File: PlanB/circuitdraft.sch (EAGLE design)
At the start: 20 parts, among them Q1 16 MHz

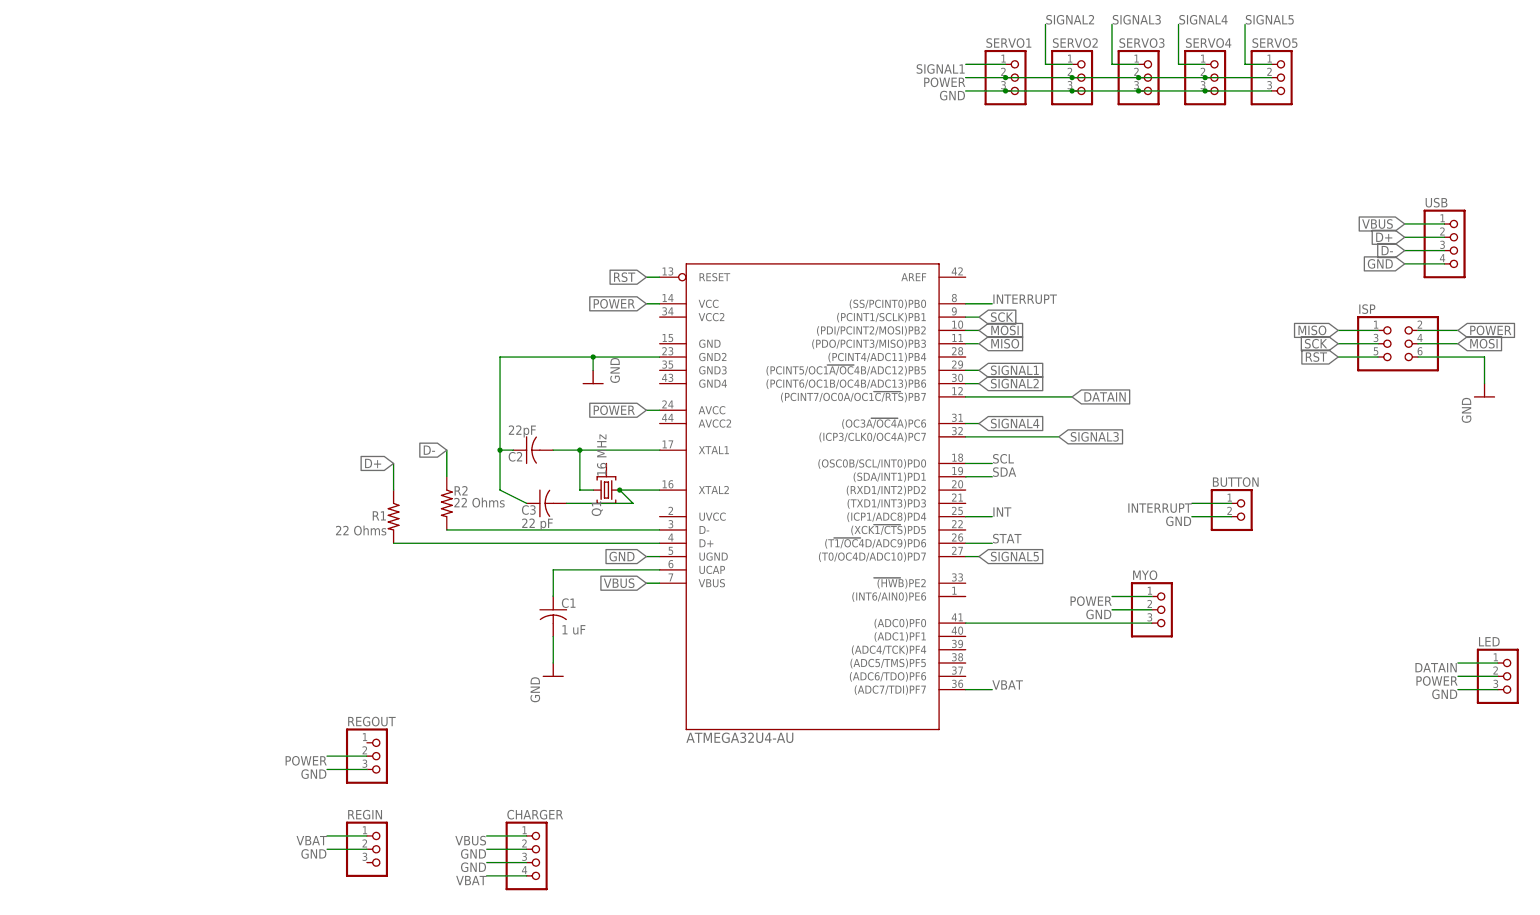
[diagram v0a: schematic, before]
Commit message: added biggnd and bigpower for large traces
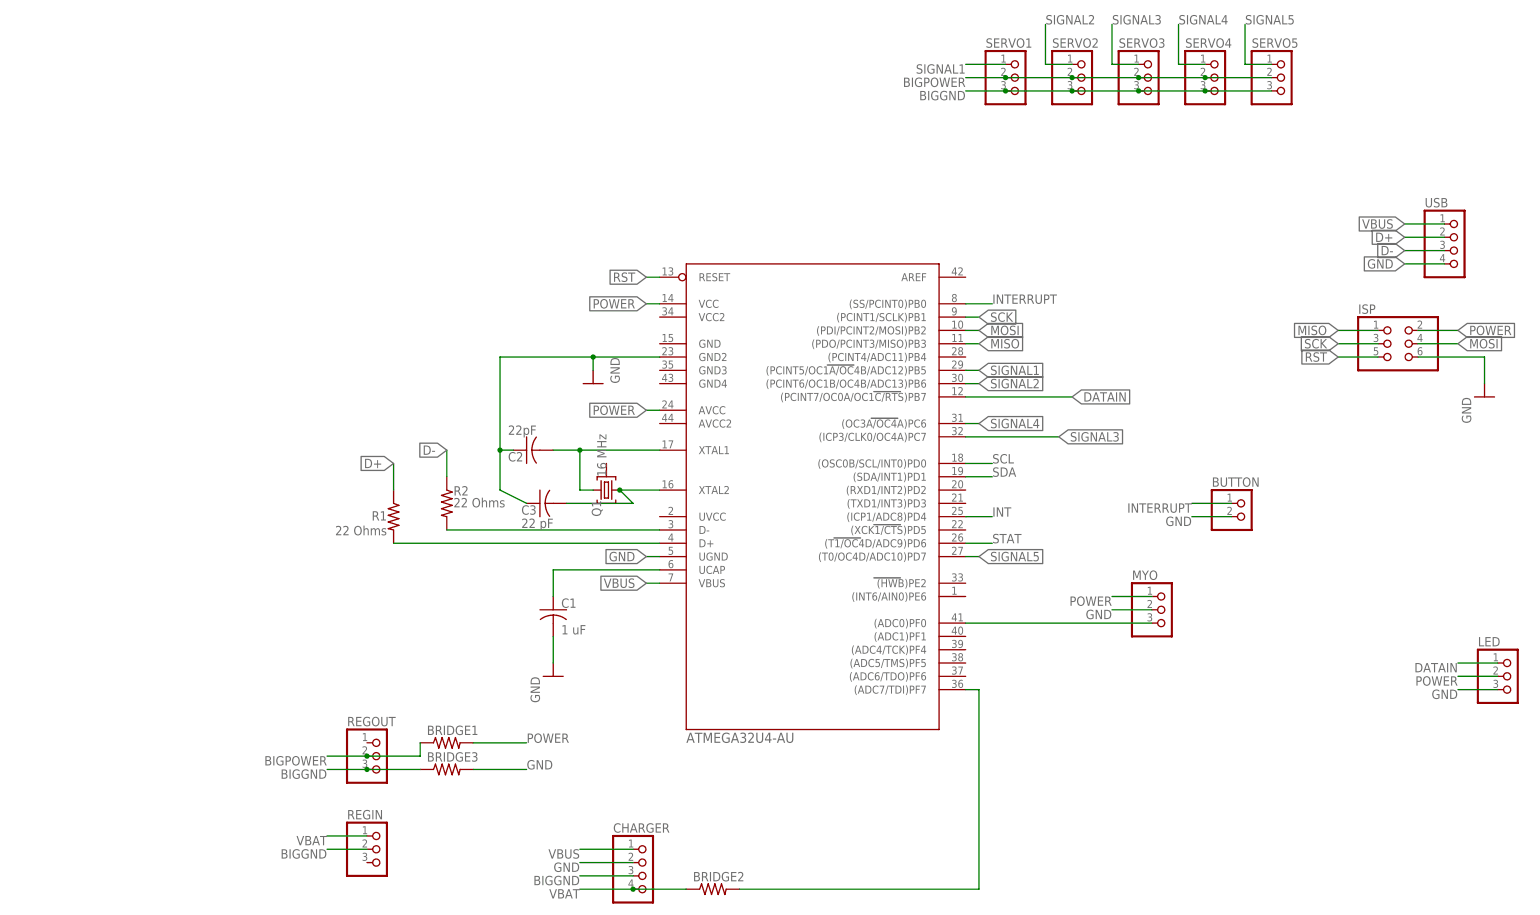
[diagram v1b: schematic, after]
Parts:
- added BRIDGE1, BRIDGE2, BRIDGE3: (no value), rcl:R-US_M0805
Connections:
- new net BIGGND: BRIDGE3.1, CHARGER.3, REGIN.2, REGOUT.3, SERVO1.3, SERVO2.3, SERVO3.3, SERVO4.3, SERVO5.3
- new net BIGPOWER: BRIDGE1.1, REGOUT.2, SERVO1.2, SERVO2.2, SERVO3.2, SERVO4.2, SERVO5.2
- new net N$9: BRIDGE2.2, U$1.(ADC7/TDI)PF7
- net GND: now also BRIDGE3.2; no longer CHARGER.3, REGIN.2, REGOUT.3, SERVO1.3, SERVO2.3, SERVO3.3, SERVO4.3, SERVO5.3
- net POWER: now also BRIDGE1.2; no longer REGOUT.2, SERVO1.2, SERVO2.2, SERVO3.2, SERVO4.2, SERVO5.2
- net VBAT: now also BRIDGE2.1; no longer U$1.(ADC7/TDI)PF7
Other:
- moved on the sheet: CHARGER

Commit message: more ajustments
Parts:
- removed BRIDGE3: (no value), rcl:R-US_M0805
- removed Q1: 16 MHz, crystal:10G7A-12.5KHZ
- removed REGIN, REGOUT: (no value), pinhead:PINHD-1X3
- added REGGNDIN, REGGNDOUT, REGVIN, REGVOUT: (no value), pinhead:PINHD-1X1
- added Y1: CY16BPS, SamacSys_Parts:CY16BPS
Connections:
- removed net BIGGND: BRIDGE3.1, CHARGER.3, REGIN.2, REGOUT.3, SERVO1.3, SERVO2.3, SERVO3.3, SERVO4.3, SERVO5.3
- net BIGPOWER: now also REGVOUT.1; no longer REGOUT.2
- net GND: now also CHARGER.3, REGGNDIN.1, REGGNDOUT.1, SERVO1.3, SERVO2.3, SERVO3.3, SERVO4.3, SERVO5.3, U$1.GND, U$1.GND3, U$1.GND4; no longer BRIDGE3.2
- net N$5: now also C2.2, U$1.XTAL1, Y1.2; no longer C3.2, Q1.1, U$1.XTAL2
- net N$6: now also C3.2, U$1.XTAL2, Y1.1; no longer C2.2, Q1.3, U$1.XTAL1
- net POWER: now also U$1.UVCC
- net VBAT: now also REGVIN.1; no longer REGIN.1
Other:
- moved on the sheet: BRIDGE1, C2, C3

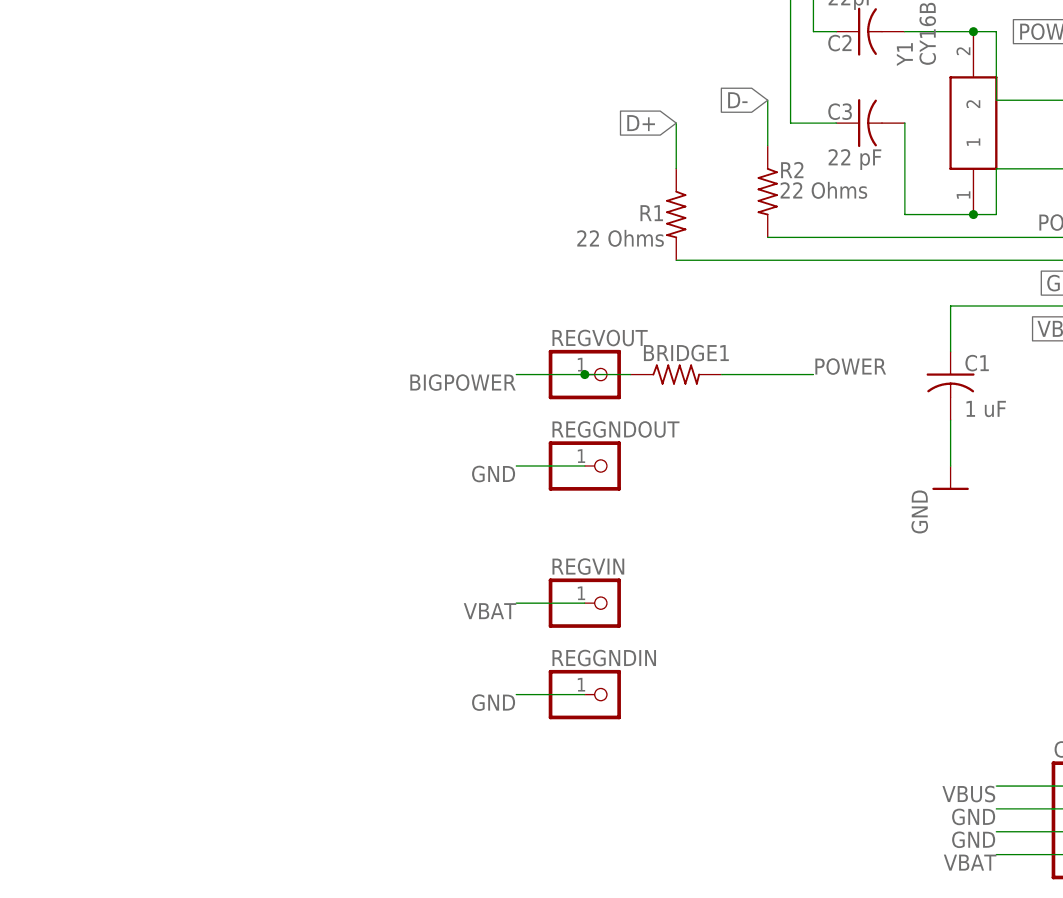
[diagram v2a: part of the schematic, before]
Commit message: refined board and fixed locations and orintations
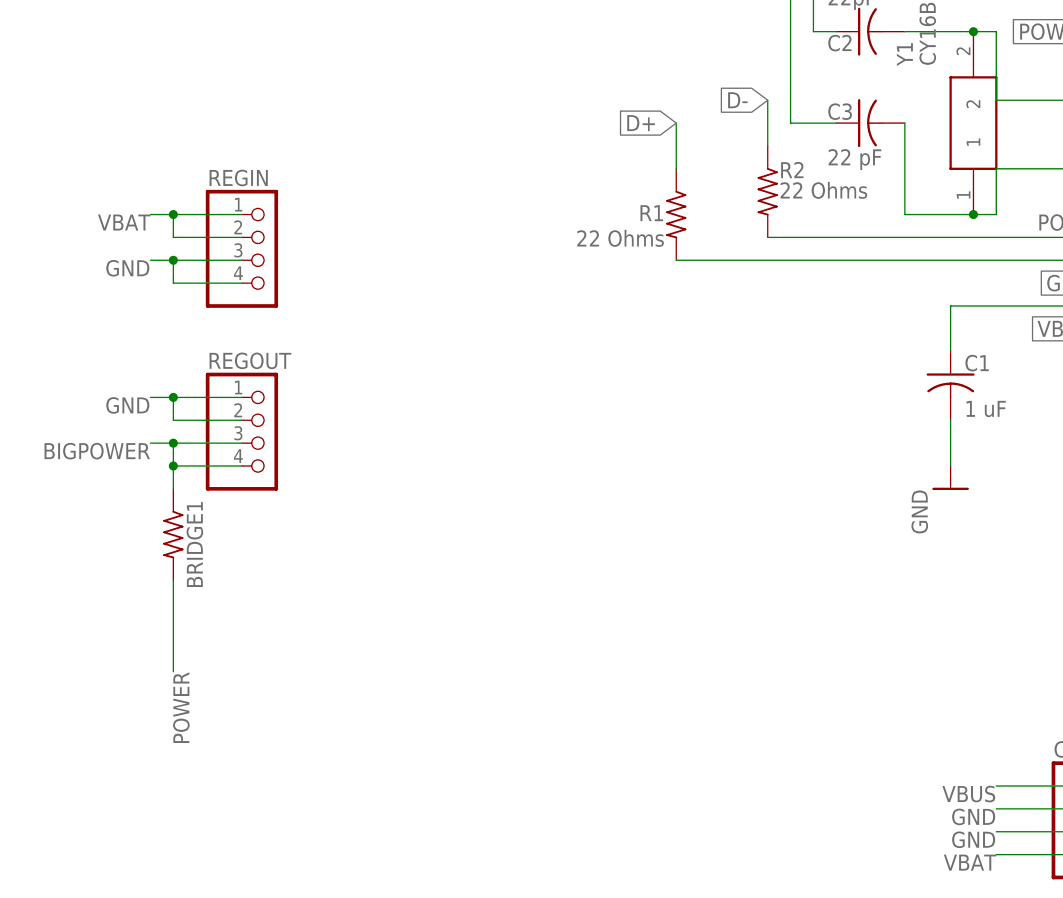
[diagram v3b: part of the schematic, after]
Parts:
- removed REGGNDIN, REGGNDOUT, REGVIN, REGVOUT: (no value), pinhead:PINHD-1X1
- added REGIN, REGOUT: (no value), pinhead:PINHD-1X4
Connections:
- net BIGPOWER: now also REGOUT.3, REGOUT.4; no longer REGVOUT.1
- net GND: now also REGIN.3, REGIN.4, REGOUT.1, REGOUT.2; no longer REGGNDIN.1, REGGNDOUT.1
- net VBAT: now also REGIN.1, REGIN.2; no longer REGVIN.1
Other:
- moved on the sheet: BRIDGE1
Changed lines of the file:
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@@
 <?xml version="1.0" encoding="utf-8"?>
 <!DOCTYPE eagle SYSTEM "eagle.dtd">
-<eagle version="9.5.1">
+<eagle version="9.5.2">
 <drawing>
 <settings>
@@
 <part name="BRIDGE1" library="rcl" library_urn="urn:adsk.eagle:library:334" deviceset="R-US_" device="M0805" package3d_urn="urn:adsk.eagle:package:23556/2"/>
 <part name="BRIDGE2" library="rcl" library_urn="urn:adsk.eagle:library:334" deviceset="R-US_" device="M0805" package3d_urn="urn:adsk.eagle:package:23556/2"/>
-<part name="REGVOUT" library="pinhead" library_urn="urn:adsk.eagle:library:325" deviceset="PINHD-1X1" device="" package3d_urn="urn:adsk.eagle:package:22485/2"/>
-<part name="REGGNDOUT" library="pinhead" library_urn="urn:adsk.eagle:library:325" deviceset="PINHD-1X1" device="" package3d_urn="urn:adsk.eagle:package:22485/2"/>
-<part name="REGVIN" library="pinhead" library_urn="urn:adsk.eagle:library:325" deviceset="PINHD-1X1" device="" package3d_urn="urn:adsk.eagle:package:22485/2"/>
-<part name="REGGNDIN" library="pinhead" library_urn="urn:adsk.eagle:library:325" deviceset="PINHD-1X1" device="" package3d_urn="urn:adsk.eagle:package:22485/2"/>
 <part name="Y1" library="SamacSys_Parts" deviceset="CY16BPS" device=""/>
+<part name="REGIN" library="pinhead" library_urn="urn:adsk.eagle:library:325" deviceset="PINHD-1X4" device="" package3d_urn="urn:adsk.eagle:package:22407/2"/>
+<part name="REGOUT" library="pinhead" library_urn="urn:adsk.eagle:library:325" deviceset="PINHD-1X4" device="" package3d_urn="urn:adsk.eagle:package:22407/2"/>
 </parts>
 <sheets>
@@
 <attribute name="VALUE" x="227.33" y="111.76" size="1.778" layer="96"/>
 </instance>
-<instance part="BRIDGE1" gate="G$1" x="86.36" y="119.38" smashed="yes">
-<attribute name="NAME" x="82.55" y="120.8786" size="1.778" layer="95"/>
-<attribute name="VALUE" x="82.55" y="116.078" size="1.778" layer="96"/>
+<instance part="BRIDGE1" gate="G$1" x="30.48" y="101.6" smashed="yes" rot="R270">
+<attribute name="NAME" x="31.9786" y="105.41" size="1.778" layer="95" rot="R270"/>
+<attribute name="VALUE" x="27.178" y="105.41" size="1.778" layer="96" rot="R270"/>
 </instance>
 <instance part="BRIDGE2" gate="G$1" x="147.32" y="66.04" smashed="yes">
@@
 <attribute name="VALUE" x="143.51" y="62.738" size="1.778" layer="96"/>
 </instance>
-<instance part="REGVOUT" gate="G$1" x="78.74" y="119.38" smashed="yes">
-<attribute name="NAME" x="72.39" y="122.555" size="1.778" layer="95"/>
-<attribute name="VALUE" x="72.39" y="114.3" size="1.778" layer="96"/>
-</instance>
-<instance part="REGGNDOUT" gate="G$1" x="78.74" y="109.22" smashed="yes">
-<attribute name="NAME" x="72.39" y="112.395" size="1.778" layer="95"/>
-<attribute name="VALUE" x="72.39" y="104.14" size="1.778" layer="96"/>
-</instance>
-<instance part="REGVIN" gate="G$1" x="78.74" y="93.98" smashed="yes">
-<attribute name="NAME" x="72.39" y="97.155" size="1.778" layer="95"/>
-<attribute name="VALUE" x="72.39" y="88.9" size="1.778" layer="96"/>
-</instance>
-<instance part="REGGNDIN" gate="G$1" x="78.74" y="83.82" smashed="yes">
-<attribute name="NAME" x="72.39" y="86.995" size="1.778" layer="95"/>
-<attribute name="VALUE" x="72.39" y="78.74" size="1.778" layer="96"/>
-</instance>
 <instance part="Y1" gate="G$1" x="119.38" y="137.16" smashed="yes" rot="R90">
 <attribute name="NAME" x="111.76" y="153.67" size="1.778" layer="95" rot="R90" align="center-left"/>
 <attribute name="VALUE" x="114.3" y="153.67" size="1.778" layer="96" rot="R90" align="center-left"/>
+</instance>
+<instance part="REGIN" gate="A" x="40.64" y="132.08" smashed="yes">
+<attribute name="NAME" x="34.29" y="140.335" size="1.778" layer="95"/>
+<attribute name="VALUE" x="34.29" y="124.46" size="1.778" layer="96"/>
+</instance>
+<instance part="REGOUT" gate="A" x="40.64" y="111.76" smashed="yes">
+<attribute name="NAME" x="34.29" y="120.015" size="1.778" layer="95"/>
+<attribute name="VALUE" x="34.29" y="104.14" size="1.778" layer="96"/>
 </instance>
 </instances>
@@
 <segment>
 <pinref part="BRIDGE1" gate="G$1" pin="2"/>
-<wire x1="91.44" y1="119.38" x2="101.6" y2="119.38" width="0.1524" layer="91"/>
-<label x="101.6" y="119.38" size="1.778" layer="95"/>
+<wire x1="30.48" y1="96.52" x2="30.48" y2="86.36" width="0.1524" layer="91"/>
+<label x="30.48" y="86.36" size="1.778" layer="95" rot="R270"/>
 </segment>
 <segment>
@@
 </segment>
 <segment>
-<pinref part="REGGNDOUT" gate="G$1" pin="1"/>
-<wire x1="76.2" y1="109.22" x2="68.58" y2="109.22" width="0.1524" layer="91"/>
-<label x="68.58" y="109.22" size="1.778" layer="95" rot="R180"/>
-</segment>
-<segment>
-<pinref part="REGGNDIN" gate="G$1" pin="1"/>
-<wire x1="76.2" y1="83.82" x2="68.58" y2="83.82" width="0.1524" layer="91"/>
-<label x="68.58" y="83.82" size="1.778" layer="95" rot="R180"/>
-</segment>
-<segment>
 <pinref part="C2" gate="G$1" pin="1"/>
 <wire x1="104.14" y1="157.48" x2="101.6" y2="157.48" width="0.1524" layer="91"/>
@@
 <wire x1="137.16" y1="162.56" x2="129.54" y2="162.56" width="0.1524" layer="91"/>
 <label x="129.54" y="162.56" size="1.778" layer="95"/>
+</segment>
+<segment>
+<pinref part="REGIN" gate="A" pin="3"/>
+<wire x1="38.1" y1="132.08" x2="30.48" y2="132.08" width="0.1524" layer="91"/>
+<pinref part="REGIN" gate="A" pin="4"/>
+<wire x1="30.48" y1="132.08" x2="27.94" y2="132.08" width="0.1524" layer="91"/>
+<wire x1="30.48" y1="132.08" x2="30.48" y2="129.54" width="0.1524" layer="91"/>
+<wire x1="30.48" y1="129.54" x2="38.1" y2="129.54" width="0.1524" layer="91"/>
+<junction x="30.48" y="132.08"/>
+<label x="27.94" y="132.08" size="1.778" layer="95" rot="R180"/>
+</segment>
+<segment>
+<pinref part="REGOUT" gate="A" pin="1"/>
+<wire x1="38.1" y1="116.84" x2="30.48" y2="116.84" width="0.1524" layer="91"/>
+<wire x1="27.94" y1="116.84" x2="30.48" y2="116.84" width="0.1524" layer="91"/>
+<pinref part="REGOUT" gate="A" pin="2"/>
+<wire x1="30.48" y1="116.84" x2="30.48" y2="114.3" width="0.1524" layer="91"/>
+<wire x1="30.48" y1="114.3" x2="38.1" y2="114.3" width="0.1524" layer="91"/>
+<junction x="30.48" y="116.84"/>
+<label x="27.94" y="116.84" size="1.778" layer="95" rot="R180"/>
 </segment>
 </net>
@@
 </segment>
 <segment>
-<pinref part="REGVIN" gate="G$1" pin="1"/>
-<wire x1="76.2" y1="93.98" x2="68.58" y2="93.98" width="0.1524" layer="91"/>
-<label x="68.58" y="93.98" size="1.778" layer="95" rot="R180"/>
+<pinref part="REGIN" gate="A" pin="1"/>
+<wire x1="38.1" y1="137.16" x2="30.48" y2="137.16" width="0.1524" layer="91"/>
+<pinref part="REGIN" gate="A" pin="2"/>
+<wire x1="30.48" y1="137.16" x2="30.48" y2="134.62" width="0.1524" layer="91"/>
+<wire x1="30.48" y1="134.62" x2="38.1" y2="134.62" width="0.1524" layer="91"/>
+<wire x1="30.48" y1="137.16" x2="27.94" y2="137.16" width="0.1524" layer="91"/>
+<junction x="30.48" y="137.16"/>
+<label x="27.94" y="137.16" size="1.778" layer="95" rot="R180"/>
 </segment>
 </net>
@@
 </segment>
 <segment>
-<pinref part="REGVOUT" gate="G$1" pin="1"/>
-<wire x1="76.2" y1="119.38" x2="68.58" y2="119.38" width="0.1524" layer="91"/>
-<label x="68.58" y="119.38" size="1.778" layer="95" rot="R180"/>
+<pinref part="REGOUT" gate="A" pin="3"/>
+<wire x1="38.1" y1="111.76" x2="30.48" y2="111.76" width="0.1524" layer="91"/>
+<pinref part="REGOUT" gate="A" pin="4"/>
+<wire x1="30.48" y1="111.76" x2="27.94" y2="111.76" width="0.1524" layer="91"/>
+<wire x1="38.1" y1="109.22" x2="30.48" y2="109.22" width="0.1524" layer="91"/>
+<wire x1="30.48" y1="109.22" x2="30.48" y2="111.76" width="0.1524" layer="91"/>
+<junction x="30.48" y="111.76"/>
+<label x="27.94" y="111.76" size="1.778" layer="95" rot="R180"/>
 <pinref part="BRIDGE1" gate="G$1" pin="1"/>
-<wire x1="76.2" y1="119.38" x2="81.28" y2="119.38" width="0.1524" layer="91"/>
-<junction x="76.2" y="119.38"/>
-</segment>
-</net>
+<wire x1="30.48" y1="109.22" x2="30.48" y2="106.68" width="0.1524" layer="91"/>
+<junction x="30.48" y="109.22"/>
+</segment>
+</net>

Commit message: final refinement
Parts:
- C1: device rcl:C-US025-024X044 -> rcl:C-US050-024X044
- R1, R2: device rcl:R-US_0204/7 -> rcl:R-US_0207/10
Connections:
- net INTERRUPT: now also U$1.(INT6/AIN0)PE6; no longer U$1.(SS/PCINT0)PB0
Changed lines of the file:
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@@
 <?xml version="1.0" encoding="utf-8"?>
 <!DOCTYPE eagle SYSTEM "eagle.dtd">
-<eagle version="9.5.2">
+<eagle version="9.5.1">
 <drawing>
 <settings>
@@
 <part name="U$1" library="mega32U4" deviceset="ATMEGA32U4-AU" device=""/>
 <part name="USB" library="pinhead" library_urn="urn:adsk.eagle:library:325" deviceset="PINHD-1X4" device="" package3d_urn="urn:adsk.eagle:package:22407/2"/>
-<part name="C1" library="rcl" library_urn="urn:adsk.eagle:library:334" deviceset="C-US" device="025-024X044" package3d_urn="urn:adsk.eagle:package:23630/1" value="1 uF"/>
+<part name="C1" library="rcl" library_urn="urn:adsk.eagle:library:334" deviceset="C-US" device="050-024X044" package3d_urn="urn:adsk.eagle:package:23643/1" value="1 uF"/>
 <part name="AGND1" library="supply1" library_urn="urn:adsk.eagle:library:371" deviceset="GND" device=""/>
-<part name="R1" library="rcl" library_urn="urn:adsk.eagle:library:334" deviceset="R-US_" device="0204/7" package3d_urn="urn:adsk.eagle:package:23498/2" value="22 Ohms"/>
-<part name="R2" library="rcl" library_urn="urn:adsk.eagle:library:334" deviceset="R-US_" device="0204/7" package3d_urn="urn:adsk.eagle:package:23498/2" value="22 Ohms"/>
+<part name="R1" library="rcl" library_urn="urn:adsk.eagle:library:334" deviceset="R-US_" device="0207/10" package3d_urn="urn:adsk.eagle:package:23491/2" value="22 Ohms"/>
+<part name="R2" library="rcl" library_urn="urn:adsk.eagle:library:334" deviceset="R-US_" device="0207/10" package3d_urn="urn:adsk.eagle:package:23491/2" value="22 Ohms"/>
 <part name="ISP" library="pinhead" library_urn="urn:adsk.eagle:library:325" deviceset="PINHD-2X3" device="" package3d_urn="urn:adsk.eagle:package:22462/2"/>
 <part name="AGND3" library="supply1" library_urn="urn:adsk.eagle:library:371" deviceset="GND" device=""/>
@@
 <net name="INTERRUPT" class="0">
 <segment>
-<pinref part="U$1" gate="G$1" pin="(SS/PCINT0)PB0"/>
-<wire x1="195.58" y1="177.8" x2="200.66" y2="177.8" width="0.1524" layer="91"/>
-<label x="200.66" y="177.8" size="1.778" layer="95"/>
-</segment>
-<segment>
 <pinref part="BUTTON" gate="G$1" pin="1"/>
 <wire x1="246.38" y1="139.7" x2="238.76" y2="139.7" width="0.1524" layer="91"/>
 <label x="238.76" y="139.7" size="1.778" layer="95" rot="R180"/>
 </segment>
-</net>
+<segment>
+<pinref part="U$1" gate="G$1" pin="(INT6/AIN0)PE6"/>
+<wire x1="195.58" y1="121.92" x2="200.66" y2="121.92" width="0.1524" layer="91"/>
+<label x="200.66" y="121.92" size="1.778" layer="95"/>
+</segment>
+</net>
